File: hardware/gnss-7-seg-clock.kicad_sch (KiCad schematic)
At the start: 90 parts, among them J1 USB4105-GF-A, J2 Conn_Coaxial, J3 Conn_01x03, SW1 SW_Push, SW2 SW_Push, SW3 SW_Push, SW4 SW_Push, SW5 SW_Push, U1 SA15-11GWA, U10 RP2040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

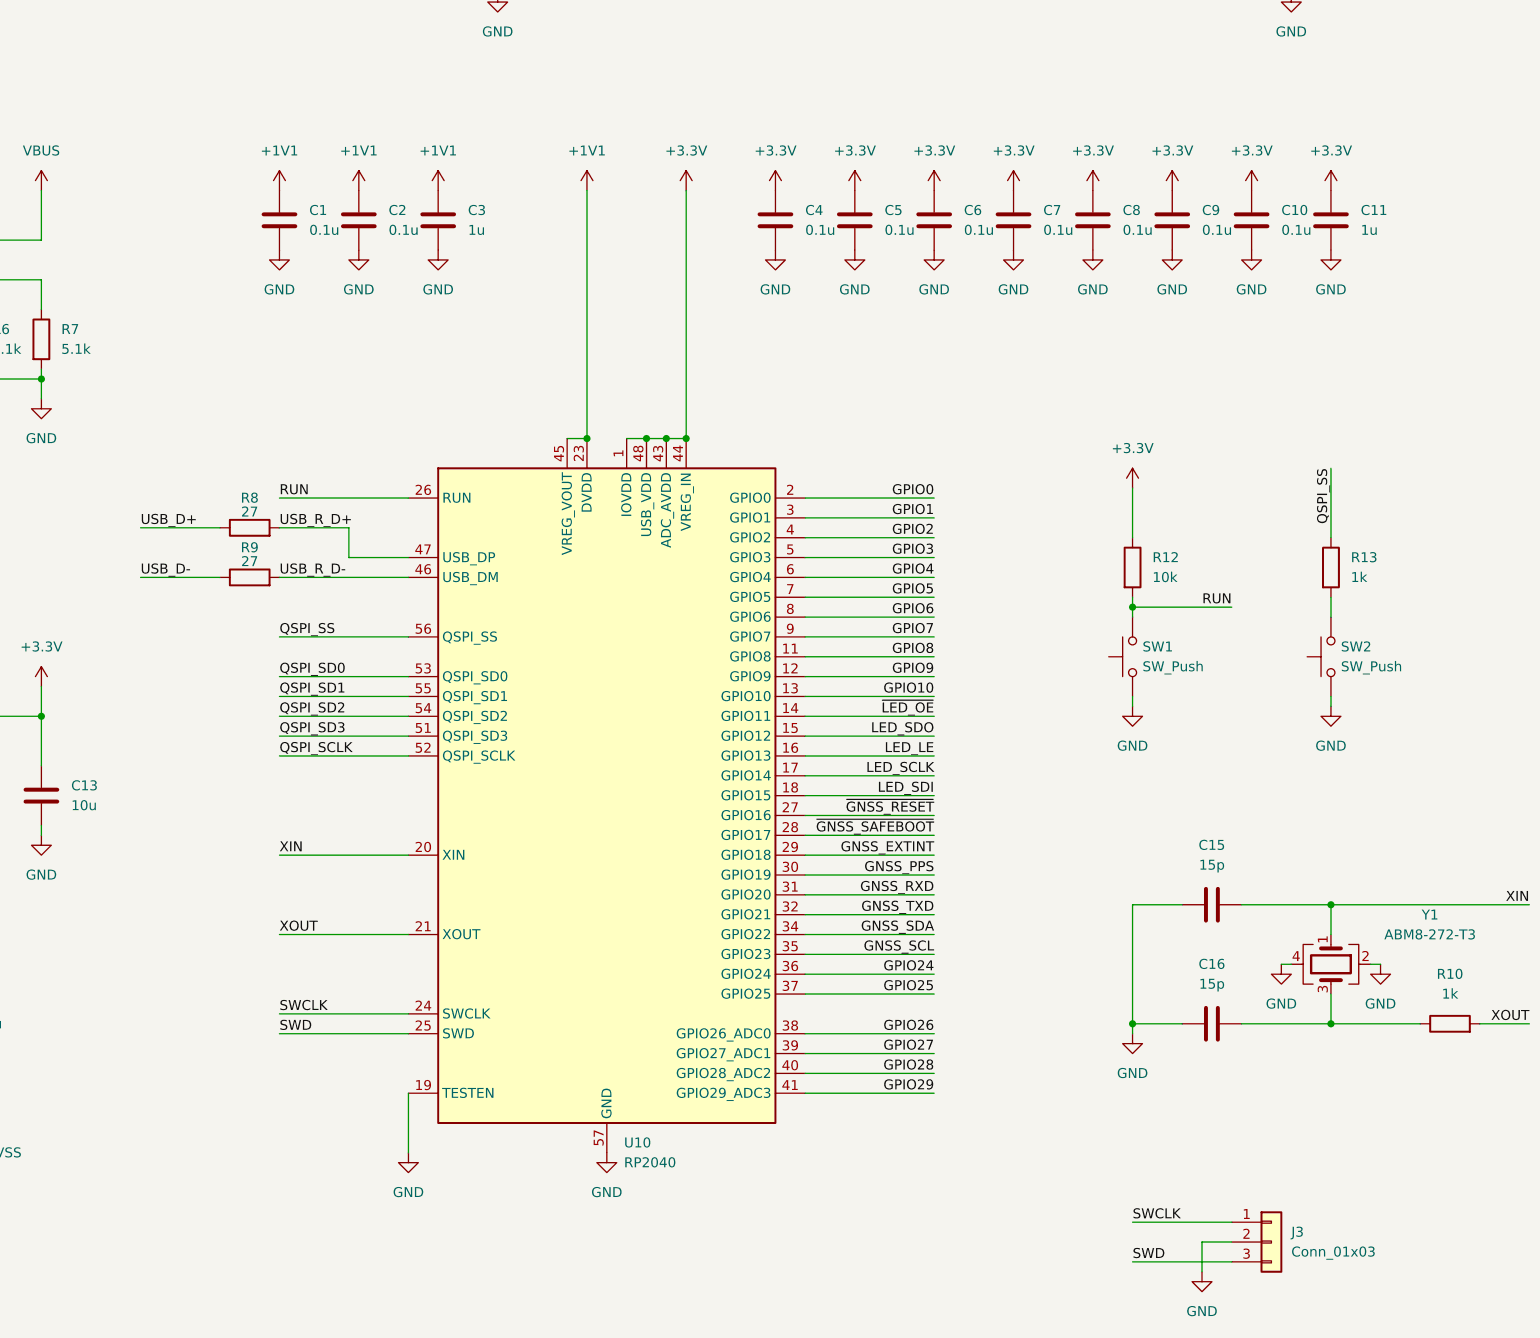
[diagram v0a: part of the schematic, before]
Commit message: Re-save project with KiCad 9.0.7
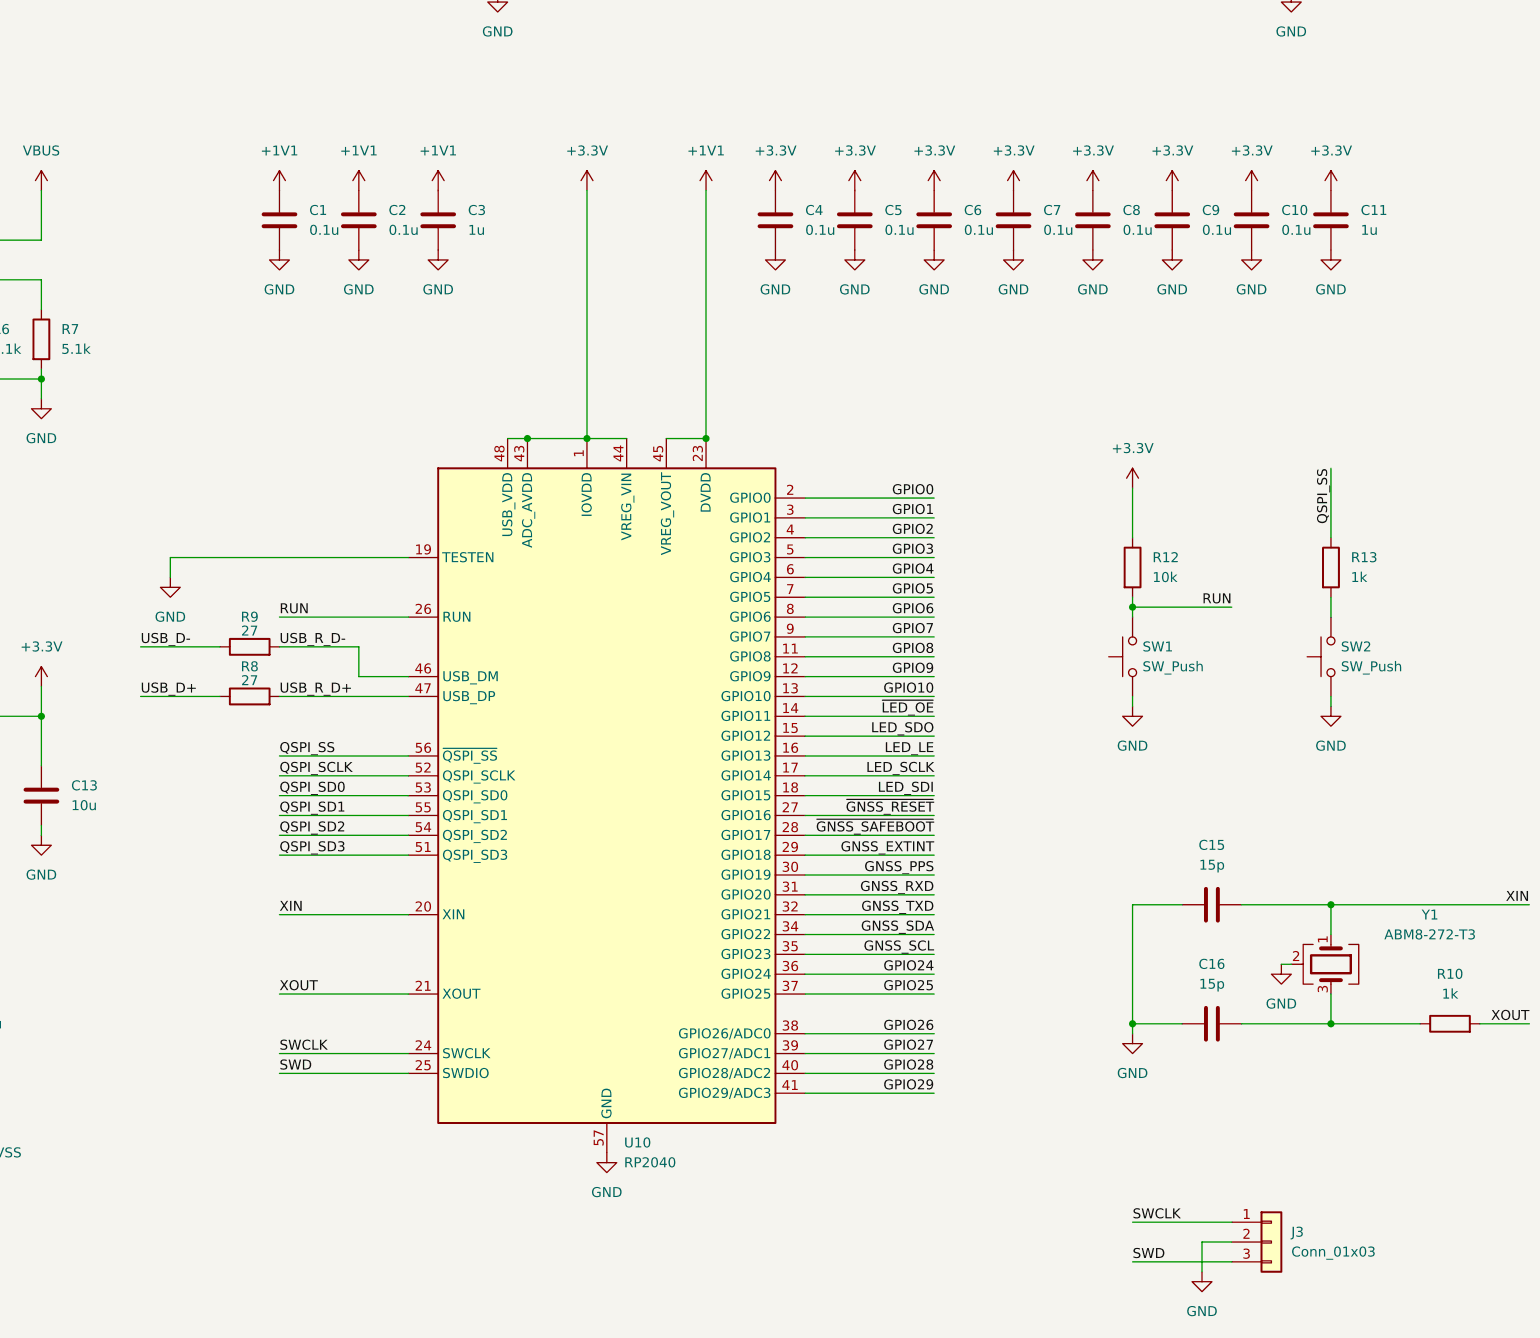
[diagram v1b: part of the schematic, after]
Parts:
- U10: footprint gnss-7-seg-clock:QFN-56-1EP_7x7mm_P0.4mm_EP3.2x3.2mm_HandSolder -> Package_DFN_QFN:QFN-56-1EP_7x7mm_P0.4mm_EP3.2x3.2mm
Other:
- moved on the sheet: R8, R9
